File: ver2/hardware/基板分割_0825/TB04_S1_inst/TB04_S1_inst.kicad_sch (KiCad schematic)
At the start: 12 parts, among them J101 USB_C_Receptacle_PowerOnly_6P, SW101 SW_SPDT, U101 74LS157, U102 74HC138

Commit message: ver2: 残り5プロジェクトの不要シートを一括削除
IF表示13/S4 10/S3 11/S1 12/S2 10枚のsheetブロックをS式単位で除去し、
対応する子シート56ファイルを削除。部分削除が要るROM_ALU・PCは残した。
残ったブロックは全てHEADとバイト一致・括弧バランス0を全数確認。

Co-Authored-By: Claude Opus 5 <noreply@anthropic.com>
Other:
- removed sheet Decoder
- removed sheet InterFace
- removed sheet PC_aluMux (4 ページ)
- removed sheet RS00
- removed sheet RS01
- removed sheet addrDecord
- removed sheet addrMUX
- removed sheet gates
- removed sheet inPort
- removed sheet outPort
- removed sheet ram
- removed sheet sp

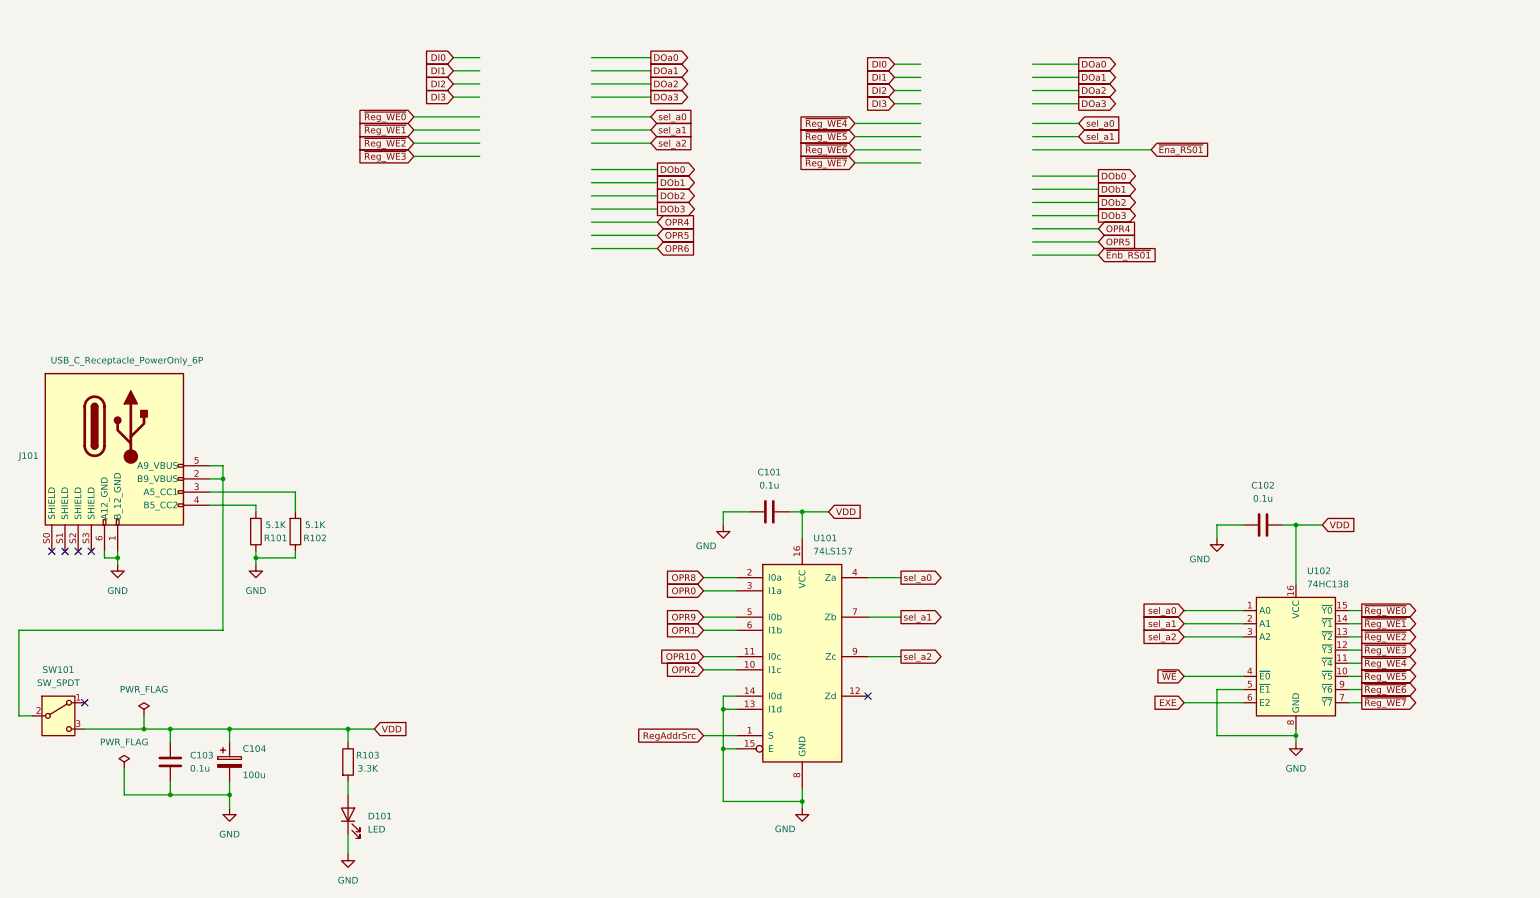
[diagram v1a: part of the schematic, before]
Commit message: ver2: S1-S4のシート内部分削除が完了(署名相違ゼロ)
ROM_ALUをS1(命令ROM側)とS2(ALU ROM・フラグ側)に、PCをS3(ALU入力MUX)と
S4(PC系)に分割。4基板1320ピンをマスターと署名比較して相違0・
ANOMALIES 0。パスコンの員数もIC数と一致(S1 7/S2 17/S3 22/S4 15)。

Co-Authored-By: Claude Opus 5 <noreply@anthropic.com>
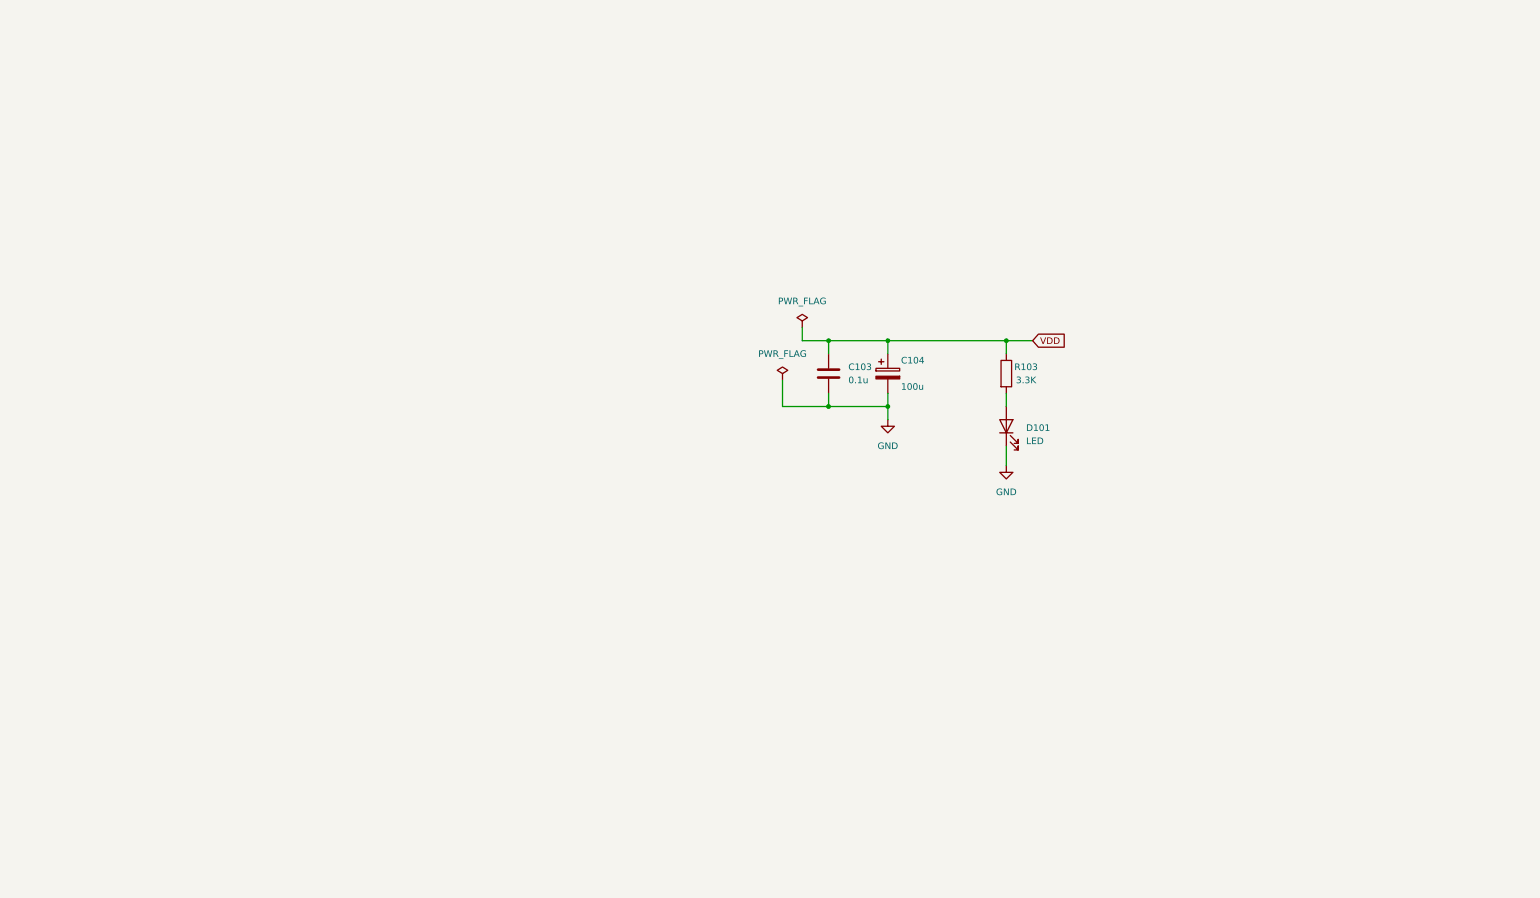
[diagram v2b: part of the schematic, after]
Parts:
- removed C101, C102: 0.1u, Capacitor_THT:C_Disc_D4.3mm_W1.9mm_P5.00mm, symbol Device:C
- removed J101: USB_C_Receptacle_PowerOnly_6P, Library:USB_C_receptacle_onlypower_tanuki, symbol New_Library:USB_C_Receptacle_PowerOnly_6P_tanuki
- removed R101, R102: 5.1K, Resistor_THT:R_Axial_DIN0207_L6.3mm_D2.5mm_P10.16mm_Horizontal, symbol Device:R
- removed SW101: SW_SPDT, Library:sw_slide, symbol Switch:SW_SPDT
- removed U101: 74LS157, symbol 74xx:74LS157
- removed U102: 74HC138, Package_DIP:DIP-16_W7.62mm_Socket, symbol 74xx:74HC138
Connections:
- no-connect marks 6 -> 0
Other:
- moved on the sheet: C103, C104, D101, R103

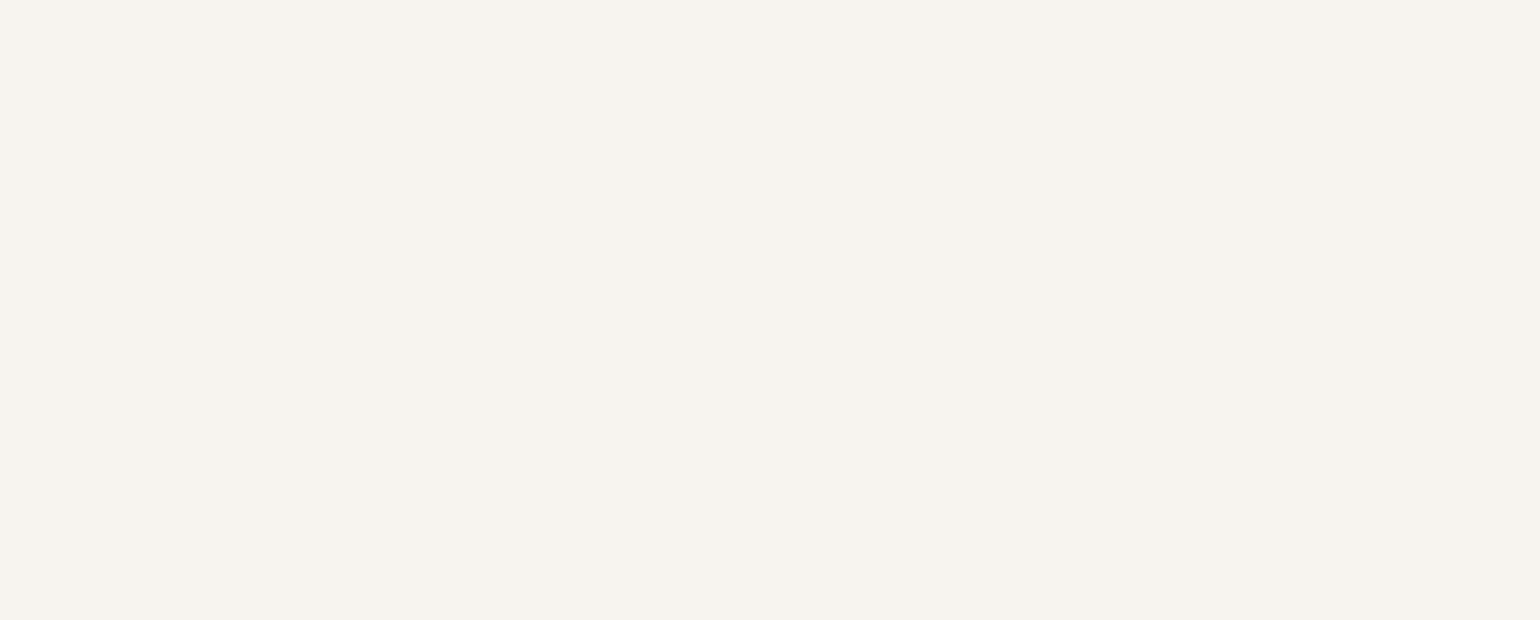
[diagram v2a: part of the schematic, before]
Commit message: ver2: S1-S4にバスヘッダ3本を実装(120ピン全数一致)／S4にIF向け20ピン3個
J101-103は4枚とも確定表と全120ピン一致。J104(IF入力)/J105(IF表示)/
J106(キャリアB)も20ピン全一致。コネクタ以外の署名はマスターと相違0で、
コネクタ追加時のワイヤ吸着なし。PC_Qはバスに載せずJ106のみ。

Co-Authored-By: Claude Opus 5 <noreply@anthropic.com>
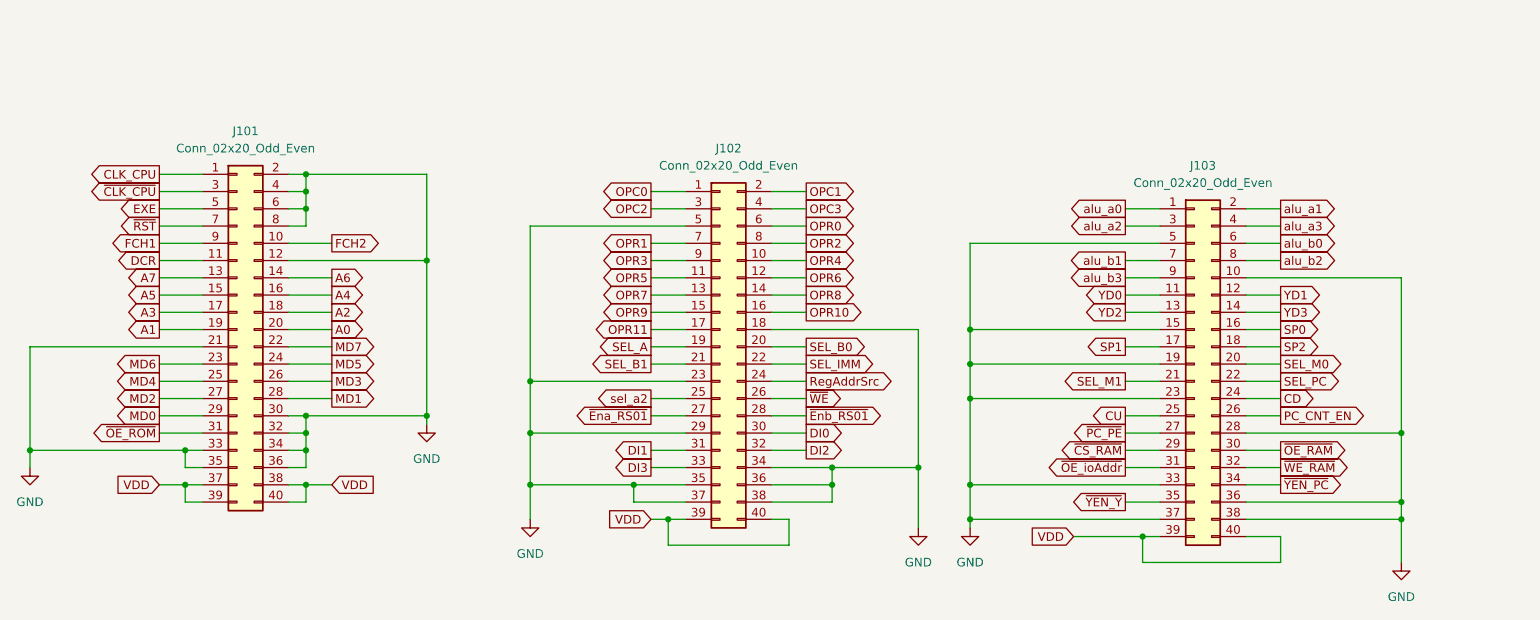
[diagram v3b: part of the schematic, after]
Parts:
- added J101, J102, J103: Conn_02x20_Odd_Even, symbol Connector_Generic:Conn_02x20_Odd_Even
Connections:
- net GND: now also J101.12 (Pin_12), J101.2 (Pin_2), J101.21 (Pin_21), J101.30 (Pin_30), J101.32 (Pin_32), J101.33 (Pin_33), J101.34 (Pin_34), J101.35 (Pin_35), J101.36 (Pin_36), J101.4 (Pin_4), J101.6 (Pin_6), J101.8 (Pin_8), J102.18 (Pin_18), J102.23 (Pin_23), J102.29 (Pin_29), J102.34 (Pin_34), J102.35 (Pin_35), J102.36 (Pin_36), J102.37 (Pin_37), J102.38 (Pin_38), J102.5 (Pin_5), J103.10 (Pin_10), J103.15 (Pin_15), J103.19 (Pin_19), J103.23 (Pin_23), J103.28 (Pin_28), J103.33 (Pin_33), J103.36 (Pin_36), J103.37 (Pin_37), J103.38 (Pin_38), J103.5 (Pin_5)
- net VDD: now also J101.37 (Pin_37), J101.38 (Pin_38), J101.39 (Pin_39), J101.40 (Pin_40), J102.39 (Pin_39), J102.40 (Pin_40), J103.39 (Pin_39), J103.40 (Pin_40)
- new net A0: J101.20 (Pin_20)
- new net A1: J101.19 (Pin_19)
- new net A2: J101.18 (Pin_18)
- new net A3: J101.17 (Pin_17)
- new net A4: J101.16 (Pin_16)
- new net A5: J101.15 (Pin_15)
- new net A6: J101.14 (Pin_14)
- new net A7: J101.13 (Pin_13)
- new net CD: J103.24 (Pin_24)
- new net CLK_CPU: J101.1 (Pin_1)
- new net CU: J103.25 (Pin_25)
- new net DCR: J101.11 (Pin_11)
- new net DI0: J102.30 (Pin_30)
- new net DI1: J102.31 (Pin_31)
- new net DI2: J102.32 (Pin_32)
- new net DI3: J102.33 (Pin_33)
- new net EXE: J101.5 (Pin_5)
- new net FCH1: J101.9 (Pin_9)
- new net FCH2: J101.10 (Pin_10)
- new net MD0: J101.29 (Pin_29)
- new net MD1: J101.28 (Pin_28)
- new net MD2: J101.27 (Pin_27)
- new net MD3: J101.26 (Pin_26)
- new net MD4: J101.25 (Pin_25)
- new net MD5: J101.24 (Pin_24)
- new net MD6: J101.23 (Pin_23)
- new net MD7: J101.22 (Pin_22)
- new net OPC0: J102.1 (Pin_1)
- new net OPC1: J102.2 (Pin_2)
- new net OPC2: J102.3 (Pin_3)
- new net OPC3: J102.4 (Pin_4)
- new net OPR0: J102.6 (Pin_6)
- new net OPR1: J102.7 (Pin_7)
- new net OPR10: J102.16 (Pin_16)
- new net OPR11: J102.17 (Pin_17)
- new net OPR2: J102.8 (Pin_8)
- new net OPR3: J102.9 (Pin_9)
- new net OPR4: J102.10 (Pin_10)
- new net OPR5: J102.11 (Pin_11)
- new net OPR6: J102.12 (Pin_12)
- new net OPR7: J102.13 (Pin_13)
- new net OPR8: J102.14 (Pin_14)
- new net OPR9: J102.15 (Pin_15)
- new net PC_CNT_EN: J103.26 (Pin_26)
- new net RegAddrSrc: J102.24 (Pin_24)
- new net SEL_A: J102.19 (Pin_19)
- new net SEL_B0: J102.20 (Pin_20)
- new net SEL_B1: J102.21 (Pin_21)
- new net SEL_IMM: J102.22 (Pin_22)
- new net SEL_M0: J103.20 (Pin_20)
- new net SEL_M1: J103.21 (Pin_21)
- new net SEL_PC: J103.22 (Pin_22)
- new net SP0: J103.16 (Pin_16)
- new net SP1: J103.17 (Pin_17)
- new net SP2: J103.18 (Pin_18)
- new net YD0: J103.11 (Pin_11)
- new net YD1: J103.12 (Pin_12)
- new net YD2: J103.13 (Pin_13)
- new net YD3: J103.14 (Pin_14)
- new net alu_a0: J103.1 (Pin_1)
- new net alu_a1: J103.2 (Pin_2)
- new net alu_a2: J103.3 (Pin_3)
- new net alu_a3: J103.4 (Pin_4)
- new net alu_b0: J103.6 (Pin_6)
- new net alu_b1: J103.7 (Pin_7)
- new net alu_b2: J103.8 (Pin_8)
- new net alu_b3: J103.9 (Pin_9)
- new net sel_a2: J102.25 (Pin_25)
- new net ~{CLK_CPU}: J101.3 (Pin_3)
- new net ~{CS_RAM}: J103.29 (Pin_29)
- new net ~{Ena_RS01}: J102.27 (Pin_27)
- new net ~{Enb_RS01}: J102.28 (Pin_28)
- new net ~{OE_RAM}: J103.30 (Pin_30)
- new net ~{OE_ROM}: J101.31 (Pin_31)
- new net ~{OE_ioAddr}: J103.31 (Pin_31)
- new net ~{PC_PE}: J103.27 (Pin_27)
- new net ~{RST}: J101.7 (Pin_7)
- new net ~{WE_RAM}: J103.32 (Pin_32)
- new net ~{WE}: J102.26 (Pin_26)
- new net ~{YEN_PC}: J103.34 (Pin_34)
- new net ~{YEN_Y}: J103.35 (Pin_35)

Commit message: ver2: キャリアに7segIF用2×5コネクタ4個と電源部を実装／全7枚に予備の端子台
- キャリア: J3-J6(2×5)が桁1-4で表と全一致・DIG_*16ネットは2ピン構成
  (isolated_pin_label 16件→0件)、C1/C2/電源LED/端子台を追加
- 入力の2×10はJ1→J2にリナンバー(20ピンの中身は表と一致)
- 7枚とも端子台J1602を1個ずつ追加(pin1=＋/pin2=GNDで向きは全枚統一)
- 署名比較で既存ピンのネット変化は7枚とも0件(吸着なし)

Co-Authored-By: Claude Opus 5 <noreply@anthropic.com>
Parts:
- added J1602: Screw_Terminal_01x02, symbol Connector:Screw_Terminal_01x02
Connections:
- net GND: now also J1602.2 (Pin_2)
- net VDD: now also J1602.1 (Pin_1)
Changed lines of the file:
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@@
 	)
 	(junction
+		(at 171.45 85.09)
+		(diameter 0)
+		(color 0 0 0 0)
+	)
+	(junction
+		(at 167.64 97.79)
+		(diameter 0)
+		(color 0 0 0 0)
+	)
+	(junction
 		(at 176.53 85.09)
 		(diameter 0)
@@
 	(wire
 		(pts
+			(xy 157.48 97.79) (xy 167.64 97.79)
+		)
+		(stroke
+			(width 0)
+			(type default)
+		)
+	)
+	(wire
+		(pts
 			(xy 240.03 181.61) (xy 267.97 181.61)
 		)
@@
 	(wire
 		(pts
+			(xy 157.48 87.63) (xy 157.48 97.79)
+		)
+		(stroke
+			(width 0)
+			(type default)
+		)
+	)
+	(wire
+		(pts
 			(xy 127 201.93) (xy 124.46 201.93)
 		)
@@
 	(wire
 		(pts
+			(xy 157.48 85.09) (xy 171.45 85.09)
+		)
+		(stroke
+			(width 0)
+			(type default)
+		)
+	)
+	(wire
+		(pts
 			(xy 175.26 189.23) (xy 198.12 189.23)
 		)
@@
 					(unit 1)
 				)
+			)
+		)
+	)
+	(symbol
+		(lib_id "Connector:Screw_Terminal_01x02")
+		(at 152.4 85.09 0)
+		(mirror y)
+		(unit 1)
+		(body_style 1)
+		(exclude_from_sim no)
+		(in_bom yes)
+		(on_board yes)
+		(in_pos_files yes)
+		(dnp no)
+		(fields_autoplaced yes)
+		(property "Reference" "J1602"
+			(at 152.4 78.74 0)
+			(show_name no)
+			(do_not_autoplace no)
+			(effects
+				(font
+					(size 1.27 1.27)
+				)
+			)
+		)
+		(property "Value" "Screw_Terminal_01x02"
+			(at 152.4 81.28 0)
+			(show_name no)
+			(do_not_autoplace no)
+			(effects
+				(font
+					(size 1.27 1.27)
+				)
+			)
+		)
+		(property "Footprint" ""
+			(at 152.4 85.09 0)
+			(hide yes)
+			(show_name no)
+			(do_not_autoplace no)
+			(effects
+				(font
+					(size 1.27 1.27)
+				)
+			)
+		)
+		(property "Datasheet" ""
+			(at 152.4 85.09 0)
+			(hide yes)
+			(show_name no)
+			(do_not_autoplace no)
+			(effects
+				(font
+					(size 1.27 1.27)
+				)
+			)
+		)
+		(property "Description" "Generic screw terminal, single row, 01x02, script generated (kicad-library-utils/schlib/autogen/connector/)"
+			(at 152.4 85.09 0)
+			(hide yes)
+			(show_name no)
+			(do_not_autoplace no)
+			(effects
+				(font
+					(size 1.27 1.27)
+				)
+			)
+		)
+		(pin "2"
+		)
+		(pin "1"
+		)
+		(instances
+			(project "TB04_S1_inst"
+				(path "/d176c79b-dced-4d01-bcec-7dfd676fcfc2"
+					(reference "J1602")
+					(unit 1)
+				)
